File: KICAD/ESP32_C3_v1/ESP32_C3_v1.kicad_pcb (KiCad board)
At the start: 2 copper layers, 32 parts, among them J1 USB Serial/JTAG, J10 Peer_UART, J2 Port_Header, J3 Grove Header, J4 ADC_Header, J5 Screw_Terminal_01x03, J6 Screw_Terminal_01x03, J7 J_AUTO (Reset Automation), J8 External 5V Power, J9 SPI (Optional Module Flash)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

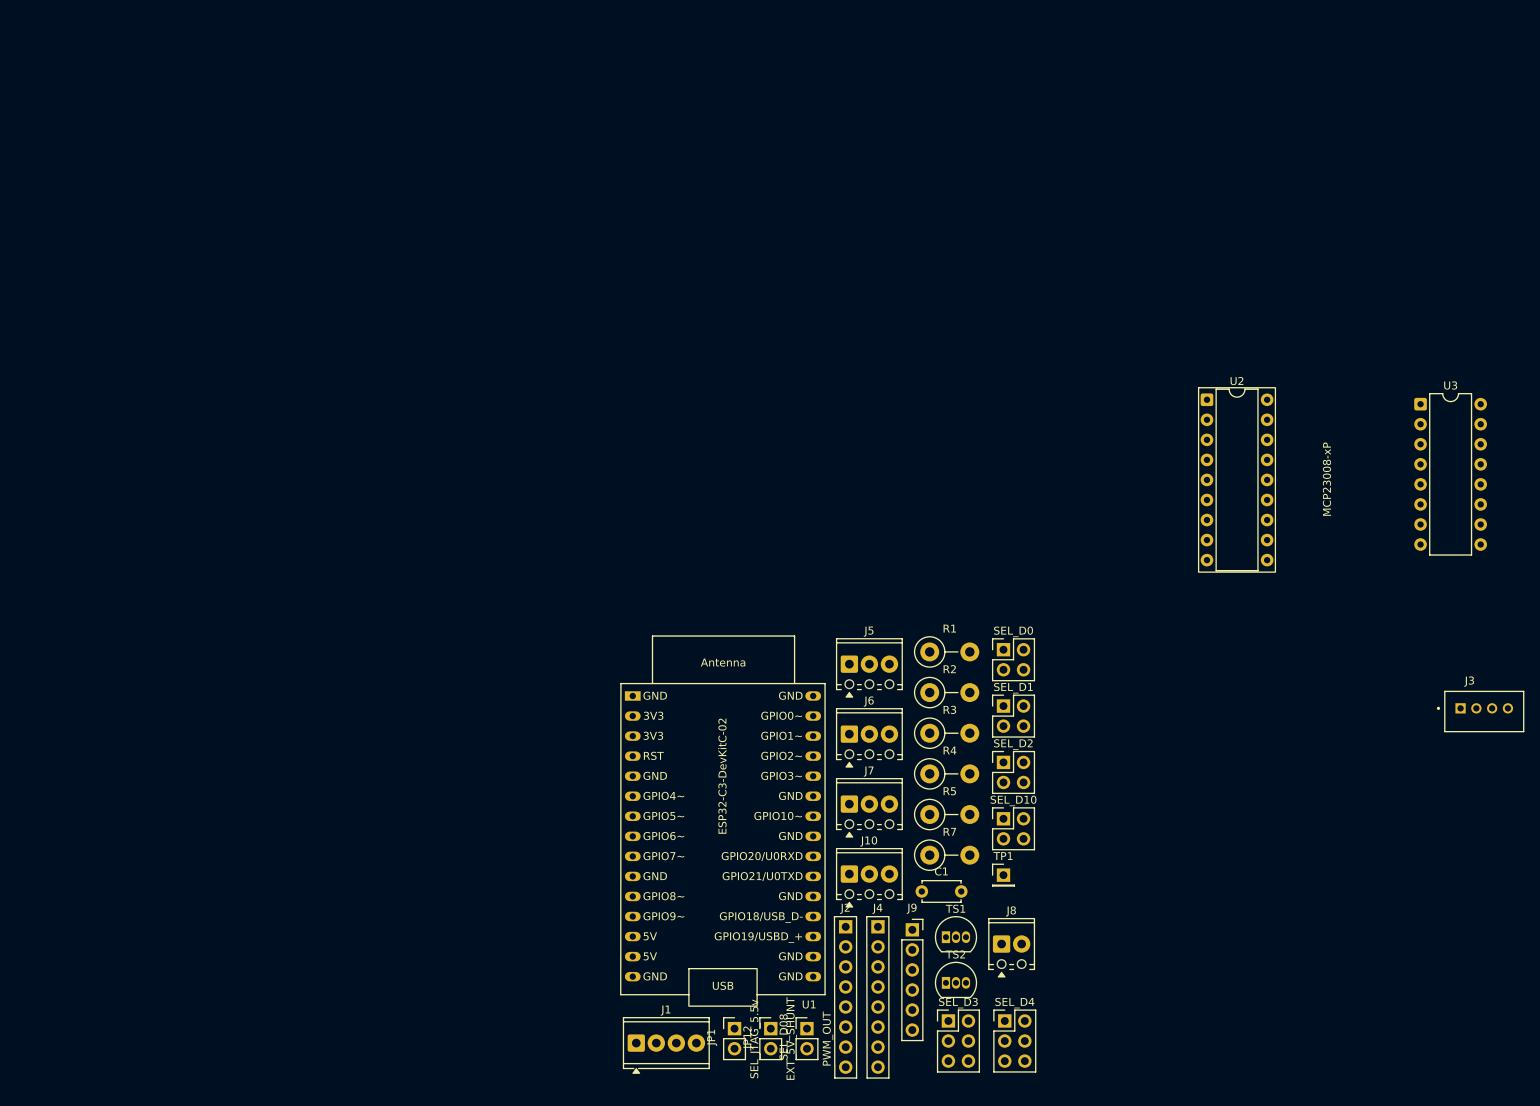
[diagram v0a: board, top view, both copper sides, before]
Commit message: Add ESP32-C3 harness v1 PCB draft
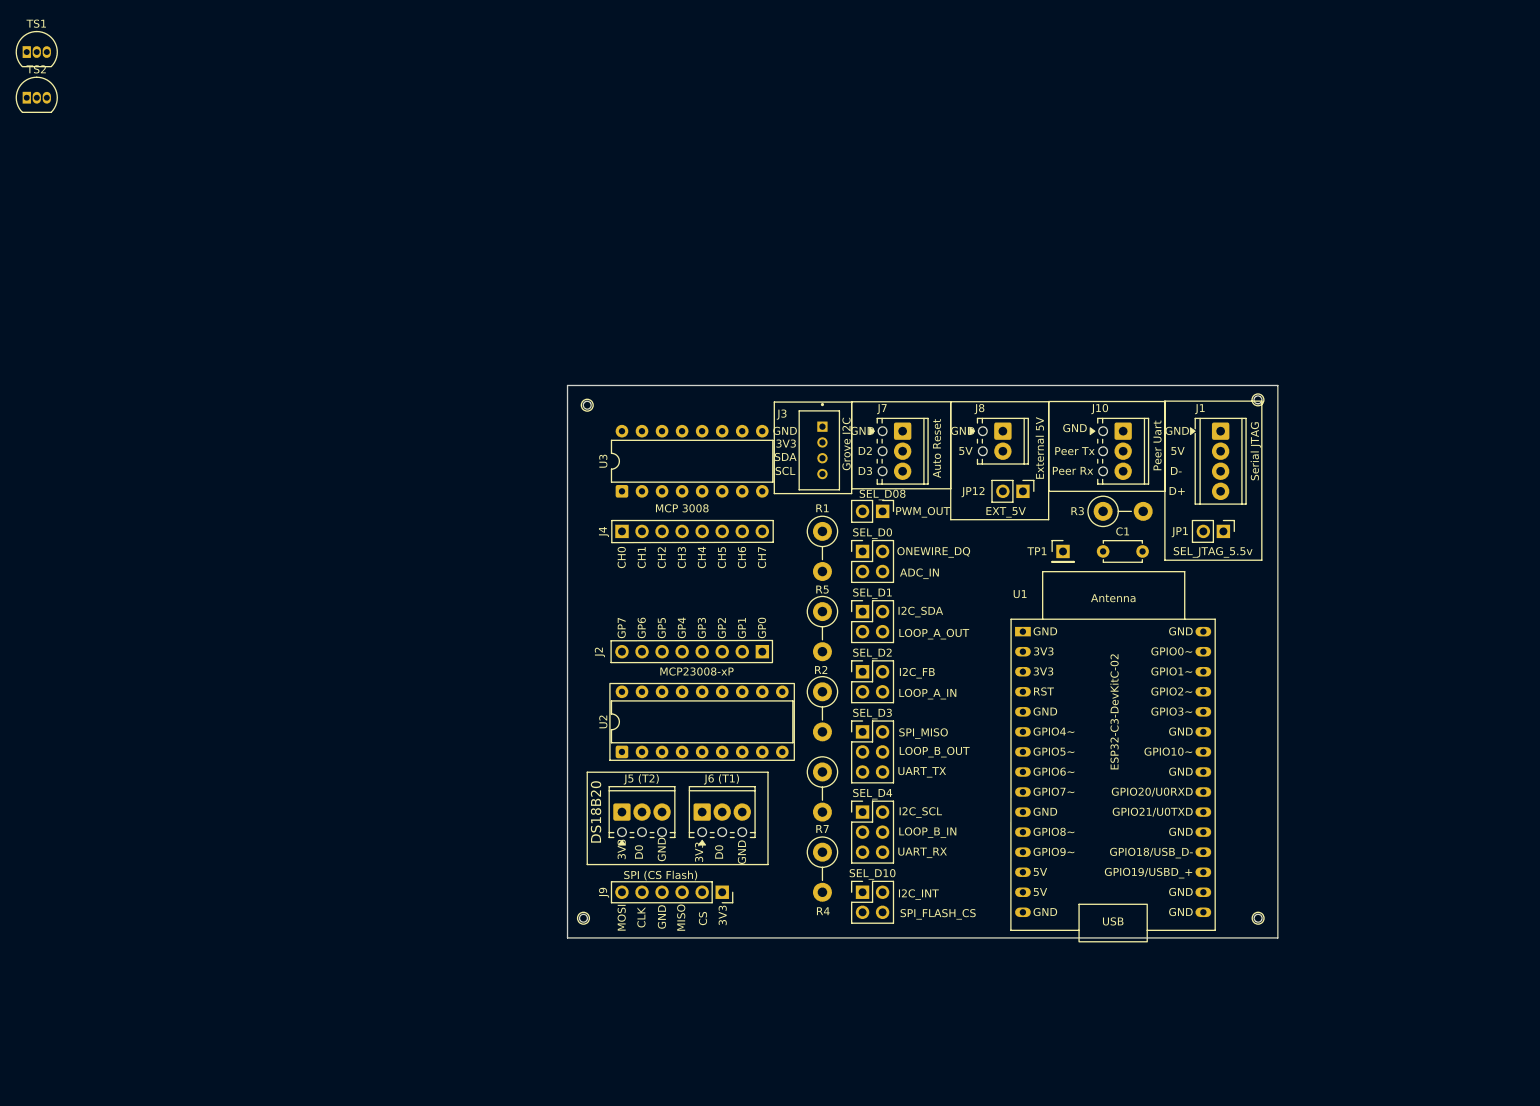
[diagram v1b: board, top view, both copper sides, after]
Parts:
- added MH1: MountingHole_1mm, ESP32_C3_Harness:MountingHole_1mm_NPTH, F.Cu at (72.5, 47.5)
- added MH2: MountingHole_1mm, ESP32_C3_Harness:MountingHole_1mm_NPTH, F.Cu at (157.5, 46.8)
- added MH3: MountingHole_1mm, ESP32_C3_Harness:MountingHole_1mm_NPTH, F.Cu at (157.5, 112.5)
- added MH3: MountingHole_1mm, ESP32_C3_Harness:MountingHole_1mm_NPTH, F.Cu at (72.0, 112.5)
- J3: value Grove Header -> Grove I2C
- J5 (T2): renamed from J5
- J6 (T1): renamed from J6
- JP12: value EXT_5V_SHUNT -> EXT_5V
- SEL_D0, SEL_D1, SEL_D10, SEL_D2: footprint ESP32_C3_Harness:PinHeader_2x02_P2.54mm_Vertical -> ESP32_C3_Harness:PinHeader_2x02_RowLetter_P2.54mm_Vertical
- SEL_D3, SEL_D4: footprint ESP32_C3_Harness:PinHeader_2x03_P2.54mm_Vertical -> ESP32_C3_Harness:PinHeader_2x03_RowLetter_P2.54mm_Vertical
- moved TS1 161.7 mm to (1.49, 2.75)
- moved TS2 161.7 mm to (1.49, 8.54)
- moved J1 107.2 mm to (152.8, 50.8), turned to -90 degrees
- moved U3 101.8 mm to (76.9, 58.4), turned to 90 degrees
- moved J3 90.0 mm to (102.3, 53.2), turned to -90 degrees
- moved JP1 88.3 mm to (153.1, 63.5), turned to -90 degrees
- moved U2 86.5 mm to (76.9, 91.4), turned to 90 degrees
- moved JP12 75.2 mm to (127.7, 58.4), turned to -90 degrees
- moved SEL_D08 66.2 mm to (109.9, 61.0), turned to -90 degrees
- moved J10 66.0 mm to (140.4, 50.8), turned to -90 degrees
- moved J8 65.0 mm to (125.2, 50.8), turned to -90 degrees
- moved J4 59.7 mm to (76.9, 63.5), turned to 90 degrees
- moved U1 50.1 mm to (127.7, 76.2)
- moved C1 48.8 mm to (137.9, 66.0)
- moved J7 47.7 mm to (112.5, 50.8), turned to -90 degrees
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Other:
- board outline added: 90 x 70 mm
- board text added: "3V3"
- board text added: "5V"
- board text added: "ADC_IN"
- board text added: "Auto Reset"
- board text added: "CH0"
- board text added: "CH1"
- board text added: "CH2"
- board text added: "CH3"
- board text added: "CH4"
- board text added: "CH5"
- board text added: "CH6"
- board text added: "CH7"
- board text added: "CLK"
- board text added: "CS"
- board text added: "D+"
- board text added: "D-"
- board text added: "D0"
- board text added: "D2"
- board text added: "D3"
- board text added: "DS18B20"
- board text added: "External 5V"
- board text added: "GND"
- board text added: "GP0"
- board text added: "GP1"
- board text added: "GP2"
- board text added: "GP3"
- board text added: "GP4"
- board text added: "GP5"
- board text added: "GP6"
- board text added: "GP7"
- board text added: "I2C_FB"
- board text added: "I2C_INT"
- board text added: "I2C_SCL"
- board text added: "I2C_SDA"
- board text added: "LOOP_A_IN"
- board text added: "LOOP_A_OUT"
- board text added: "LOOP_B_IN"
- board text added: "LOOP_B_OUT"
- board text added: "MCP 3008"
- board text added: "MISO"
- board text added: "MOSI"
- board text added: "ONEWIRE_DQ"
- board text added: "Peer Rx"
- board text added: "Peer Tx"
- board text added: "Peer Uart"
- board text added: "Perfboard guide grid: 31 x 26, 2.54mm pitch"
- board text added: "SCL"
- board text added: "SDA"
- board text added: "SPI (CS Flash)"
- board text added: "SPI_FLASH_CS"
- board text added: "SPI_MISO"
- board text added: "Serial JTAG"
- board text added: "UART_RX"
- board text added: "UART_TX"

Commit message: Add ESP32-C3 PCB wirewrap silkscreen guide
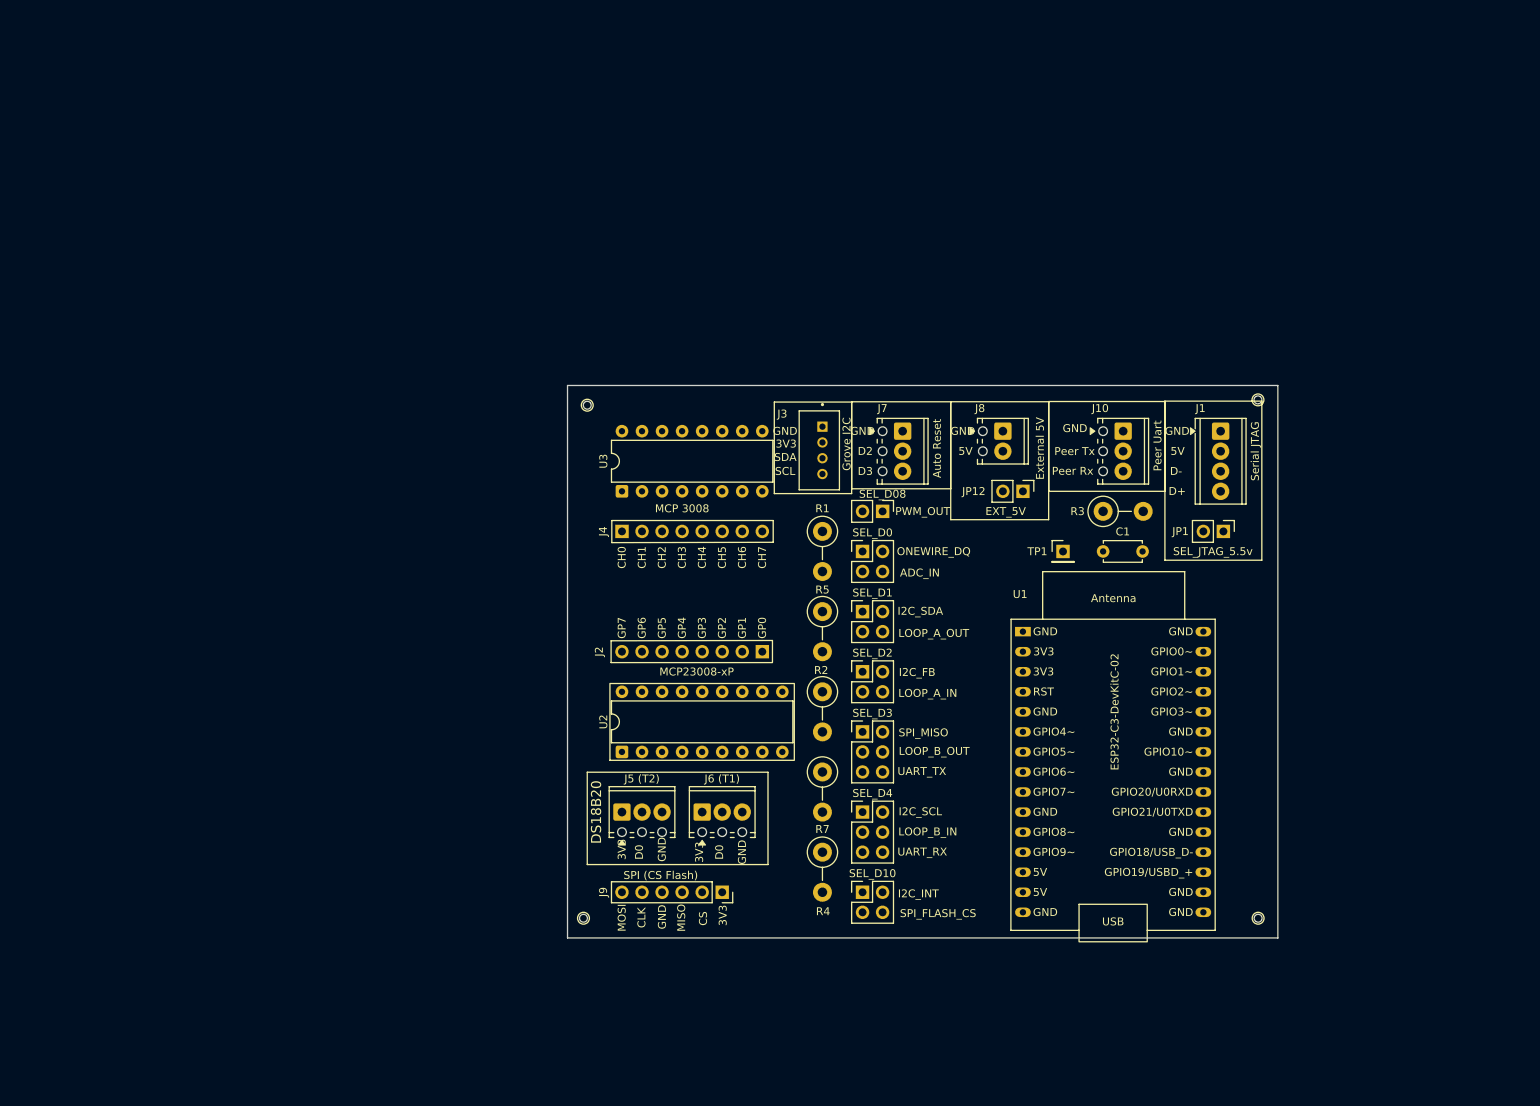
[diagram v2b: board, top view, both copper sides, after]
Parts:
- removed TS1, TS2: DS18B20, Package_TO_SOT_THT:TO-92_Inline
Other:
- board text added: "A0"
- board text added: "A1"
- board text added: "A2"
- board text added: "AGND"
- board text added: "C1"
- board text added: "CS/SHDN"
- board text added: "D1"
- board text added: "D10"
- board text added: "D4"
- board text added: "D8"
- board text added: "DGND"
- board text added: "Din"
- board text added: "Dout"
- board text added: "GPIO0"
- board text added: "GPIO1"
- board text added: "GPIO10"
- board text added: "GPIO18/USBD_-"
- board text added: "GPIO19/USBD_+"
- board text added: "GPIO2"
- board text added: "GPIO20/U0RXD"
- board text added: "GPIO21/U0TXD"
- board text added: "GPIO3"
- board text added: "GPIO4"
- board text added: "GPIO5"
- board text added: "GPIO6"
- board text added: "GPIO7"
- board text added: "GPIO8/RGB_LED"
- board text added: "GPIO9"
- board text added: "Grove I2C"
- board text added: "INT"
- board text added: "JP1"
- board text added: "MCP23008-xP"
- board text added: "NC"
- board text added: "R1"
- board text added: "R2"
- board text added: "R3"
- board text added: "R4"
- board text added: "R5"
- board text added: "R7"
- board text added: "RESET"
- board text added: "RST"
- board text added: "TP1"
- board text added: "VDD"
- board text added: "Vdd"
- board text added: "Vref"
- board text added: "Wirewrap generated U1/U2/U3 pin labels"
- board text added: "r"

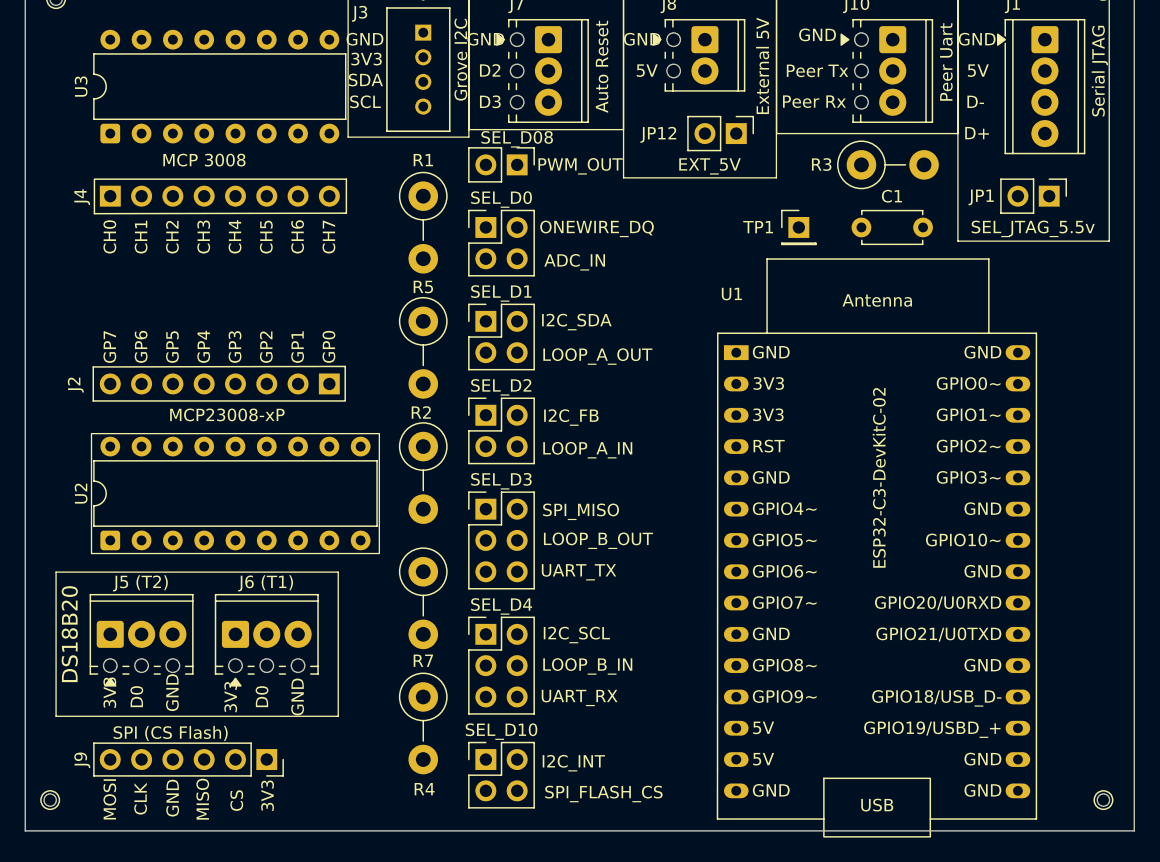
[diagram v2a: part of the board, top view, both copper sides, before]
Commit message: Add ESP32-C3 schematic v1.1 UART crosslink
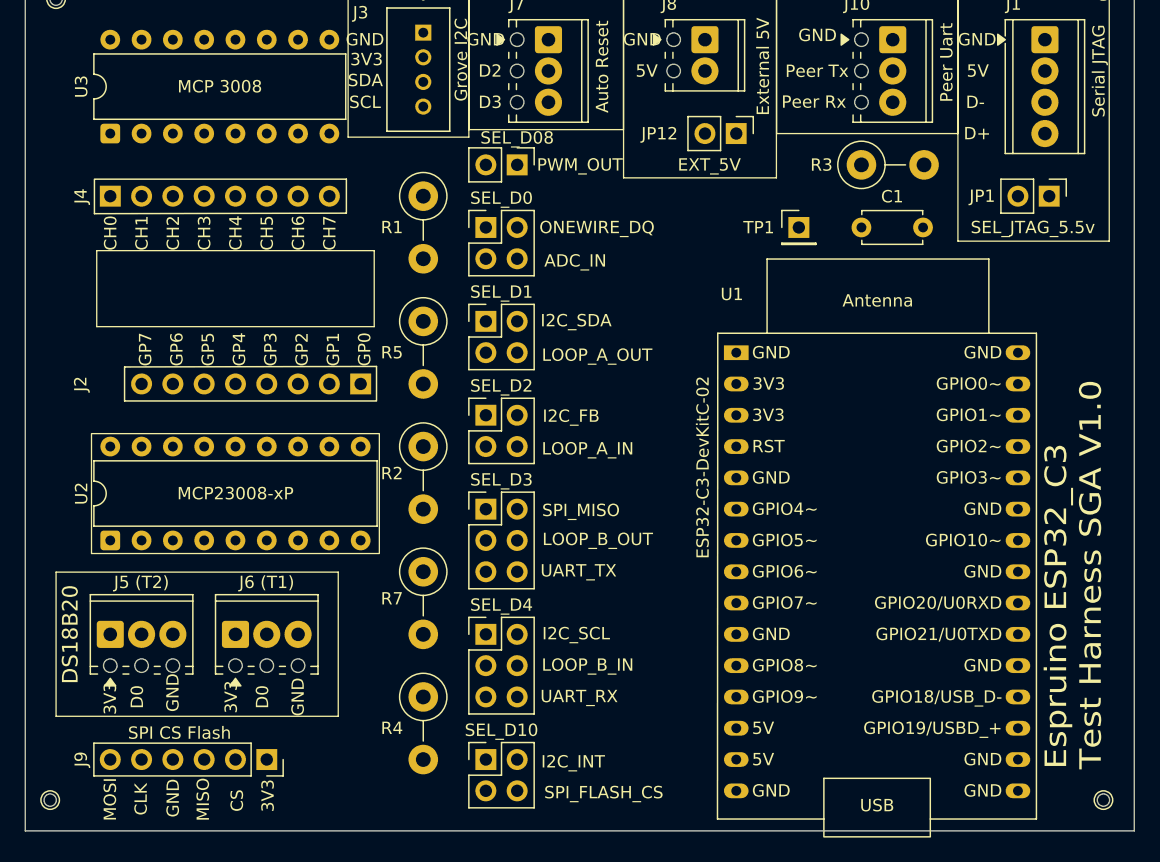
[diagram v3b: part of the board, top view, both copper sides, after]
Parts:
- moved J2 2.54 mm to (97.2, 78.7)
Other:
- board text added: "Espruino ESP32_C3 Test Harness SGA V1.0"
- board text added: "GPIO8 /LED"
- board text added: "SPI CS Flash"
- board text added: "U0RXD 20"
- board text added: "U0TXD 21"
- board text added: "USBD_+ 19"
- board text added: "USBD_- 18"
- board text removed: "CS/SHDN"
- board text removed: "GPIO18/USBD_-"
- board text removed: "GPIO19/USBD_+"
- board text removed: "GPIO20/U0RXD"
- board text removed: "GPIO21/U0TXD"
- board text removed: "GPIO8/RGB_LED"
- board text removed: "VDD"
